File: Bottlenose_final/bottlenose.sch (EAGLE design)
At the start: 9 parts, among them Q1 IRF620

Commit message: Update with miker's new stuff.
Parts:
- removed LED1: (no value), led:LED3MM
- added U$4: NCP1402, bottlenose:NCP1402
- G1: value SL-340/P3.6V -> CR1/2; device battery:SL-340/P3.6V -> battery:CR1/2
- U$2: value MCP73831SOT23-5 -> LIPO_MINIUSB; device bottlenose:MCP73831SOT23-5 -> bottlenose:LIPO_MINIUSB
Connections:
- removed net N$16: LED1.C, U$2.STAT
- removed net N$17: U$2.PROG
- removed net N$19: LED1.A
- removed net N$7: JP1.4, U$1.+5V, U$2.VDD
- new net N$10: G1.-, U$2.BAT-
- new net N$2: JP1.1, JP1.4, U$1.+5V, U$1.GND
- net GND: no longer G1.-, JP1.1, U$1.GND, U$2.VSS
- net N$14: now also U$2.BAT+; no longer U$2.VBAT
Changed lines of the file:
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@@
 <part name="P+2" library="supply1" deviceset="VCC" device=""/>
 <part name="R1" library="docu-dummy" deviceset="R" device=""/>
-<part name="U$2" library="bottlenose" deviceset="MCP73831" device="SOT23-5"/>
-<part name="G1" library="battery" deviceset="SL-340/P3.6V" device=""/>
-<part name="R2" library="docu-dummy" deviceset="R" device="" value="2kΩ">
-<attribute name="RESISTANCE" value="2kΩ"/>
-</part>
-<part name="LED1" library="led" deviceset="LED" device="3MM"/>
-<part name="R3" library="docu-dummy" deviceset="R" device="">
-<attribute name="RESISTANCE" value="470Ω"/>
-</part>
 <part name="GND1" library="supply1" deviceset="GND" device=""/>
 <part name="U$3" library="bottlenose" deviceset="MLX90614" device=""/>
-<part name="GND2" library="supply1" deviceset="GND" device=""/>
+<part name="U$2" library="bottlenose" deviceset="LIPO_MINIUSB" device=""/>
+<part name="U$4" library="bottlenose" deviceset="NCP1402" device=""/>
+<part name="G1" library="battery" deviceset="CR1/2" device=""/>
 </parts>
 <sheets>
@@
 <instance part="P+2" gate="VCC" x="68.58" y="25.4" rot="R90"/>
 <instance part="R1" gate="G$1" x="78.74" y="25.4" rot="R180"/>
-<instance part="U$2" gate="MCP73831" x="190.5" y="81.28" rot="R270"/>
-<instance part="G1" gate="G$1" x="180.34" y="93.98"/>
-<instance part="R2" gate="G$1" x="203.2" y="81.28" rot="R270">
-<attribute name="RESISTANCE" x="203.2" y="81.28" size="1.778" layer="96" rot="R270"/>
-</instance>
-<instance part="LED1" gate="G$1" x="200.66" y="63.5" rot="R90"/>
-<instance part="R3" gate="G$1" x="190.5" y="63.5">
-<attribute name="RESISTANCE" x="190.5" y="63.5" size="1.778" layer="96"/>
-</instance>
 <instance part="GND1" gate="1" x="160.02" y="48.26" rot="R270"/>
 <instance part="U$3" gate="G$1" x="185.42" y="48.26" rot="R180"/>
-<instance part="GND2" gate="1" x="167.64" y="91.44"/>
+<instance part="U$2" gate="G$1" x="228.6" y="119.38" rot="R180"/>
+<instance part="U$4" gate="G$1" x="208.28" y="93.98" rot="R270"/>
+<instance part="G1" gate="1" x="185.42" y="111.76" rot="R90"/>
 </instances>
 <busses>
@@
 <pinref part="COIL" gate="G$1" pin="2"/>
 <wire x1="48.26" y1="45.72" x2="48.26" y2="43.18" width="0.1524" layer="91"/>
+<junction x="48.26" y="45.72"/>
 </segment>
 </net>
@@
 <pinref part="GND1" gate="1" pin="GND"/>
 <wire x1="180.34" y1="48.26" x2="162.56" y2="48.26" width="0.1524" layer="91"/>
-</segment>
-<segment>
-<pinref part="U$2" gate="MCP73831" pin="VSS"/>
-<wire x1="190.5" y1="93.98" x2="190.5" y2="99.06" width="0.1524" layer="91"/>
-<wire x1="190.5" y1="99.06" x2="203.2" y2="99.06" width="0.1524" layer="91"/>
-<wire x1="203.2" y1="86.36" x2="203.2" y2="99.06" width="0.1524" layer="91"/>
-<pinref part="U$1" gate="G$1" pin="GND"/>
-<wire x1="142.24" y1="101.6" x2="142.24" y2="93.98" width="0.1524" layer="91"/>
-<wire x1="142.24" y1="93.98" x2="86.36" y2="93.98" width="0.1524" layer="91"/>
-<wire x1="86.36" y1="93.98" x2="86.36" y2="68.58" width="0.1524" layer="91"/>
-<wire x1="86.36" y1="68.58" x2="104.14" y2="68.58" width="0.1524" layer="91"/>
-<pinref part="JP1" gate="A" pin="1"/>
-<pinref part="G1" gate="G$1" pin="-"/>
-<wire x1="142.24" y1="93.98" x2="167.64" y2="93.98" width="0.1524" layer="91"/>
-<wire x1="167.64" y1="93.98" x2="175.26" y2="93.98" width="0.1524" layer="91"/>
-<wire x1="190.5" y1="99.06" x2="167.64" y2="99.06" width="0.1524" layer="91"/>
-<wire x1="167.64" y1="99.06" x2="167.64" y2="93.98" width="0.1524" layer="91"/>
-<pinref part="GND2" gate="1" pin="GND"/>
-<junction x="167.64" y="93.98"/>
 </segment>
 </net>
@@
 </segment>
 </net>
-<net name="N$16" class="0">
+<net name="N$14" class="0">
 <segment>
-<pinref part="U$2" gate="MCP73831" pin="STAT"/>
-<wire x1="195.58" y1="93.98" x2="205.74" y2="93.98" width="0.1524" layer="91"/>
-<wire x1="205.74" y1="93.98" x2="205.74" y2="63.5" width="0.1524" layer="91"/>
-<pinref part="LED1" gate="G$1" pin="C"/>
+<pinref part="U$2" gate="G$1" pin="BAT+"/>
+<pinref part="G1" gate="1" pin="+"/>
+<wire x1="190.5" y1="116.84" x2="185.42" y2="116.84" width="0.1524" layer="91"/>
+<wire x1="208.28" y1="86.36" x2="177.8" y2="86.36" width="0.1524" layer="91"/>
+<wire x1="177.8" y1="86.36" x2="177.8" y2="116.84" width="0.1524" layer="91"/>
+<wire x1="177.8" y1="116.84" x2="185.42" y2="116.84" width="0.1524" layer="91"/>
 </segment>
 </net>
-<net name="N$17" class="0">
+<net name="N$10" class="0">
 <segment>
-<pinref part="U$2" gate="MCP73831" pin="PROG"/>
-<wire x1="203.2" y1="68.58" x2="195.58" y2="68.58" width="0.1524" layer="91"/>
-<wire x1="203.2" y1="68.58" x2="203.2" y2="76.2" width="0.1524" layer="91"/>
+<pinref part="G1" gate="1" pin="-"/>
+<wire x1="208.28" y1="88.9" x2="185.42" y2="88.9" width="0.1524" layer="91"/>
+<wire x1="185.42" y1="88.9" x2="185.42" y2="106.68" width="0.1524" layer="91"/>
+<pinref part="U$2" gate="G$1" pin="BAT-"/>
+<wire x1="190.5" y1="109.22" x2="187.96" y2="106.68" width="0.1524" layer="91"/>
+<wire x1="187.96" y1="106.68" x2="185.42" y2="106.68" width="0.1524" layer="91"/>
 </segment>
 </net>
-<net name="N$19" class="0">
-<segment>
-<pinref part="LED1" gate="G$1" pin="A"/>
-<wire x1="198.12" y1="63.5" x2="195.58" y2="63.5" width="0.1524" layer="91"/>
-</segment>
-</net>
-<net name="N$14" class="0">
-<segment>
-<pinref part="U$2" gate="MCP73831" pin="VBAT"/>
-<pinref part="G1" gate="G$1" pin="+"/>
-</segment>
-</net>
-<net name="N$7" class="0">
+<net name="N$2" class="0">
 <segment>
 <wire x1="185.42" y1="53.34" x2="185.42" y2="68.58" width="0.1524" layer="91"/>
@@
 <wire x1="149.86" y1="68.58" x2="134.62" y2="68.58" width="0.1524" layer="91"/>
 <pinref part="JP1" gate="A" pin="4"/>
-<pinref part="U$2" gate="MCP73831" pin="VDD"/>
 <wire x1="185.42" y1="68.58" x2="149.86" y2="68.58" width="0.1524" layer="91"/>
+<wire x1="195.58" y1="68.58" x2="185.42" y2="68.58" width="0.1524" layer="91"/>
+<wire x1="208.28" y1="91.44" x2="195.58" y2="91.44" width="0.1524" layer="91"/>
+<wire x1="195.58" y1="91.44" x2="195.58" y2="68.58" width="0.1524" layer="91"/>
+<pinref part="U$1" gate="G$1" pin="GND"/>
+<wire x1="142.24" y1="101.6" x2="142.24" y2="93.98" width="0.1524" layer="91"/>
+<wire x1="142.24" y1="93.98" x2="86.36" y2="93.98" width="0.1524" layer="91"/>
+<wire x1="86.36" y1="93.98" x2="86.36" y2="68.58" width="0.1524" layer="91"/>
+<wire x1="86.36" y1="68.58" x2="104.14" y2="68.58" width="0.1524" layer="91"/>
+<pinref part="JP1" gate="A" pin="1"/>
+<wire x1="195.58" y1="91.44" x2="142.24" y2="91.44" width="0.1524" layer="91"/>
+<wire x1="142.24" y1="91.44" x2="142.24" y2="93.98" width="0.1524" layer="91"/>
+<junction x="195.58" y="91.44"/>
+<junction x="142.24" y="93.98"/>
+<junction x="149.86" y="68.58"/>
+<junction x="185.42" y="68.58"/>
 </segment>
 </net>

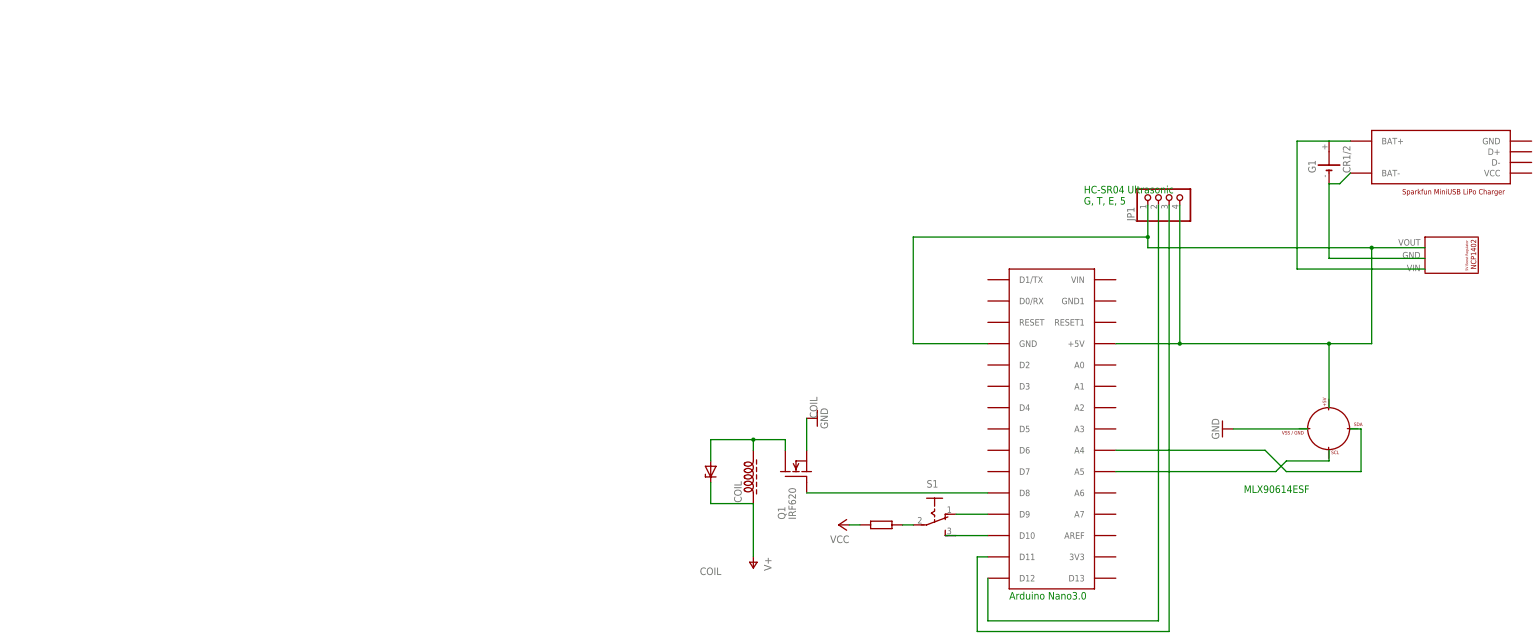
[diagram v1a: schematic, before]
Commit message: 
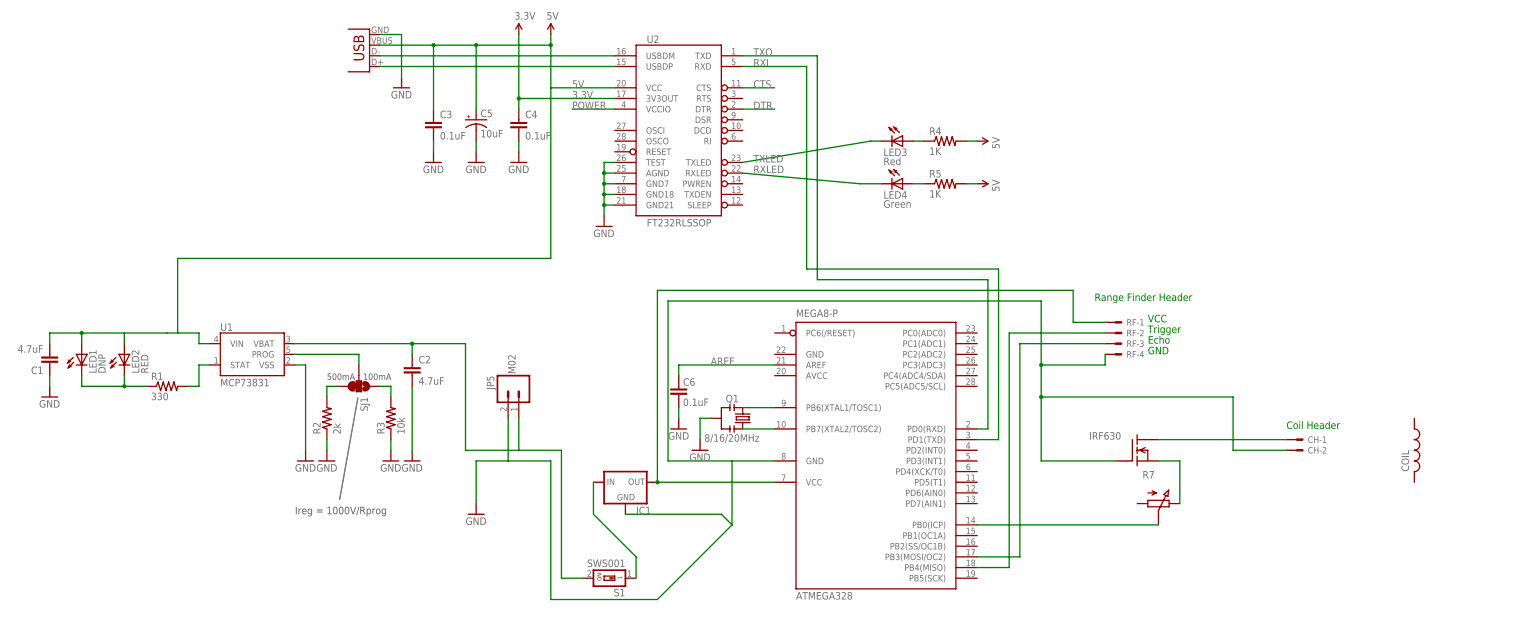
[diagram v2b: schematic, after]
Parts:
- removed G1: CR1/2, battery:CR1/2
- removed JP1: (no value), pinhead:PINHD-1X4
- removed U$1: ARDUINONANO, jet-lib:ARDUINONANO
- removed U$2: LIPO_MINIUSB, bottlenose:LIPO_MINIUSB
- removed U$3: MLX90614, bottlenose:MLX90614
- removed U$4: NCP1402, bottlenose:NCP1402
- added ATMEGA328: MEGA8-P, atmel:MEGA8-P
- added C1, C2: 4.7uF, SparkFun:CAP0402-CAP
- added C3, C4, C6: 0.1uF, SparkFun:CAP0402-CAP
- added C5: 10uF, SparkFun:CAP_POL1206
- added CH: 22-23-2021, con-molex:22-23-2021
- added IC1: (no value), v-reg:78LXX
- added IRF630: IRF620, transistor-fet:IRF620
- added JP5: M02, SparkFun:M02PTH
- added LED1: DNP, SparkFun:LED3MM
- added LED2: RED, SparkFun:LED0603
- added LED3: Red, SparkFun:LED0603
- added LED4: Green, SparkFun:LED0603
- added R1: 330, SparkFun:RESISTOR0402-RES
- added R2: 2k, SparkFun:RESISTOR0402-RES
- added R3: 10k, SparkFun:RESISTOR0402-RES
- added R4, R5: 1K, SparkFun:RESISTOR0402-RES
- added R7: (no value), pot-vitrohm:PC25
- added RF: 22-23-2041, con-molex:22-23-2041
- added SJ1: (no value), SparkFun:SOLDERJUMPER_2WAYS
- added U1: MCP73831, SparkFun:MCP73831
- added U2: FT232RLSSOP, SparkFun:FT232RLSSOP
- added X1: USB-SMD-NS, SparkFun:USB-SMD-NS
- COIL: device inductor-neosid:Z15/25CCW -> rcl:L-US0204/7
- Q1: value IRF620 -> 8/16/20MHz; device transistor-fet:IRF620 -> SparkFun:RESONATORSMD
- S1: value (none) -> SWS001; device switch:255SB -> smd-special:SWS001
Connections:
- removed net N$14: G1.+, U$2.BAT+
- removed net N$6: JP1.3, U$1.D11
- new net 3.3V: C4.1, U2.3V3OUT
- new net 5V: C1.2, C3.1, C5.+, LED1.A, LED2.A, R4.2, R5.2, U1.VIN, U2.VCC, X1.VBUS
- new net AREF: ATMEGA328.AREF, C6.2
- new net CTS: U2.CTS
- new net DTR: U2.DTR
- new net N$15: LED3.A, R4.1
- new net N$16: LED4.A, R5.1
- new net N$35: ATMEGA328.VCC@1, IC1.OUT, RF-1.S
- new net N$7: R3.2, SJ1.1
- new net POWER: U2.VCCIO
- new net PROG: SJ1.2, U1.PROG
- new net RXI: ATMEGA328.PD1(TXD), U2.RXD
- new net RXLED: LED4.C, U2.RXLED
- new net TXLED: LED3.C, U2.TXLED
- new net TXO: ATMEGA328.PD0(RXD), U2.TXD
- new net USB_D+: U2.USBDP, X1.D+
- new net USB_D-: U2.USBDM, X1.D-
- new net VBAT: C2.1, JP5.1, S1.2, U1.VBAT
- net GND: now also ATMEGA328.GND@1, C1.1, C2.2, C3.2, C4.2, C5.-, C6.1, CH-2.S, IC1.GND, IRF630.G, JP5.2, Q1.2, R2.1, R3.1, RF-4.S, U1.VSS, U2.AGND, U2.GND18, U2.GND21, U2.GND7, U2.TEST, X1.GND; no longer Q1.S
- net N$1: now also IRF630.S, R7.E; no longer Q1.G, U$1.D8
- net N$10: now also ATMEGA328.PB0(ICP), R7.S; no longer G1.-, U$2.BAT-
- net N$11: now also CH-1.S, IRF630.D; no longer S1.P
- net N$12: now also ATMEGA328.PB7(XTAL2/TOSC2), Q1.1; no longer S1.O, U$1.D9
- net N$13: now also ATMEGA328.PB6(XTAL1/TOSC1), Q1.3; no longer S1.S, U$1.D10
- net N$2: now also R1.2, U1.STAT; no longer JP1.1, JP1.4, U$1.+5V, U$1.GND
- net N$3: now also LED1.C, LED2.C, R1.1; no longer U$1.A4
- net N$4: now also R2.2, SJ1.3; no longer COIL.2, Q1.D
- net N$5: now also IC1.IN, S1.1; no longer JP1.2, U$1.D12
- net N$8: now also ATMEGA328.PB3(MOSI/OC2), RF-3.S; no longer COIL.1
- net N$9: now also ATMEGA328.PB4(MISO), RF-2.S; no longer U$1.A5
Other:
- note added: "100mA"
- note added: "500mA"
- note added: "Coil Header"
- note added: "Echo"
- note added: "GND"
- note added: "Ireg = 1000V/Rprog"
- note added: "Range Finder Header"
- note added: "Trigger"
- note added: "VCC"
- note removed: "Arduino Nano3.0"
- note removed: "HC-SR04 Ultrasonic G, T, E, 5"
- note removed: "MLX90614ESF"
